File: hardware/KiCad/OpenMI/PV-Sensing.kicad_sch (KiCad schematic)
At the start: 16 parts

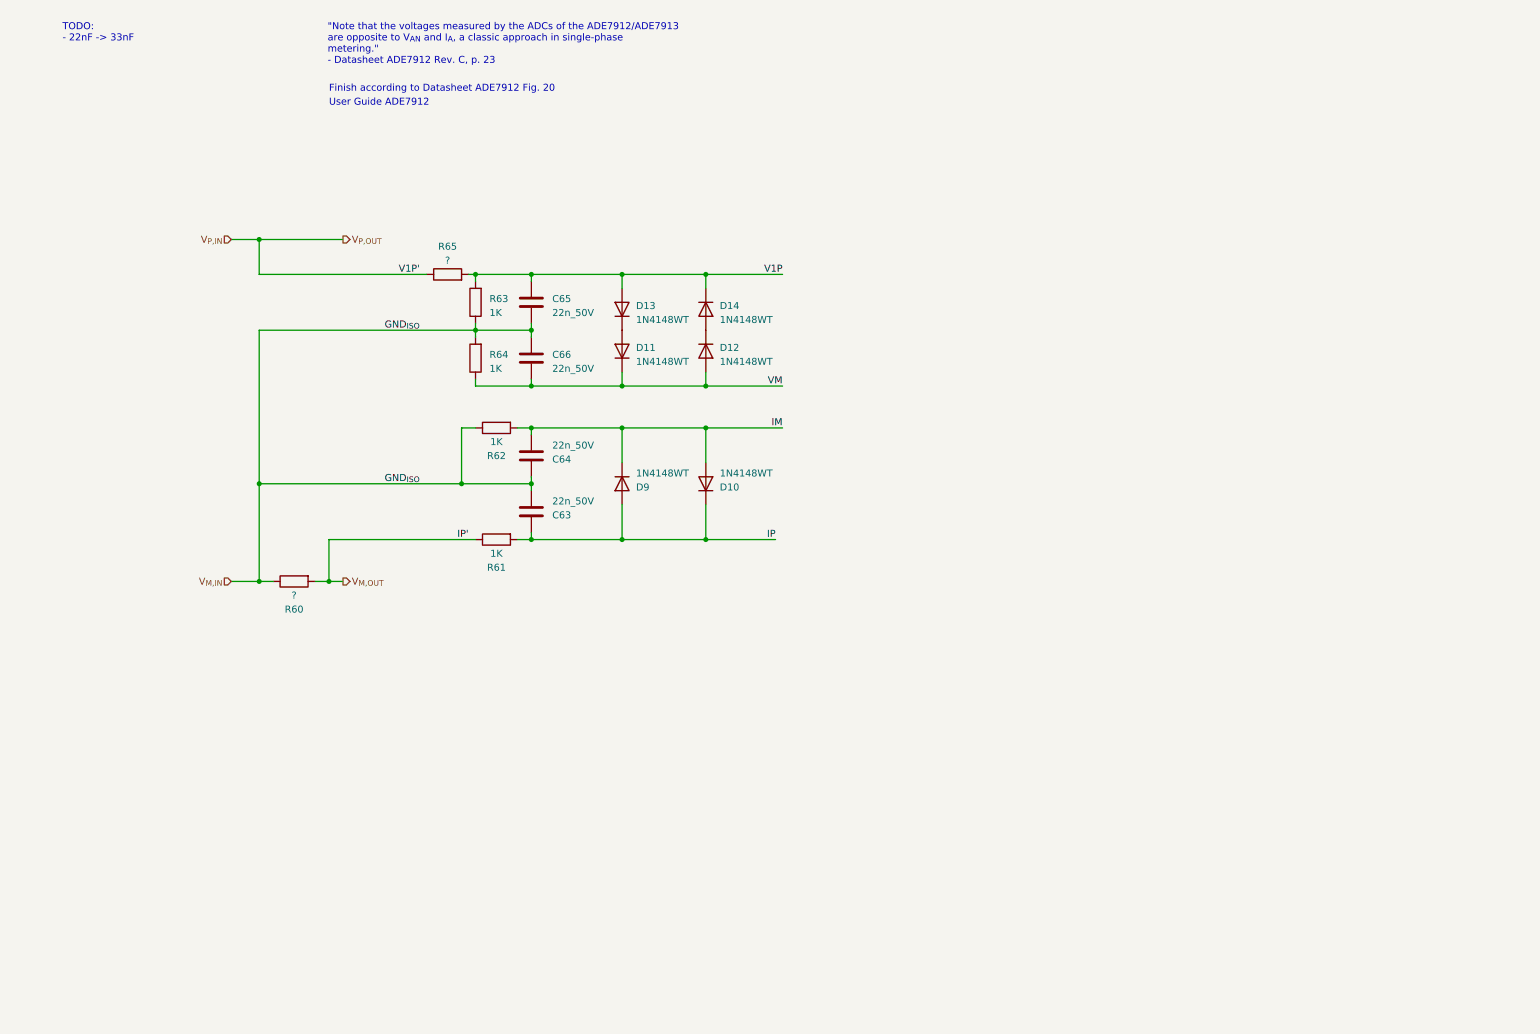
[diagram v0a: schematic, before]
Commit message: Adds specific values for sense resistors.
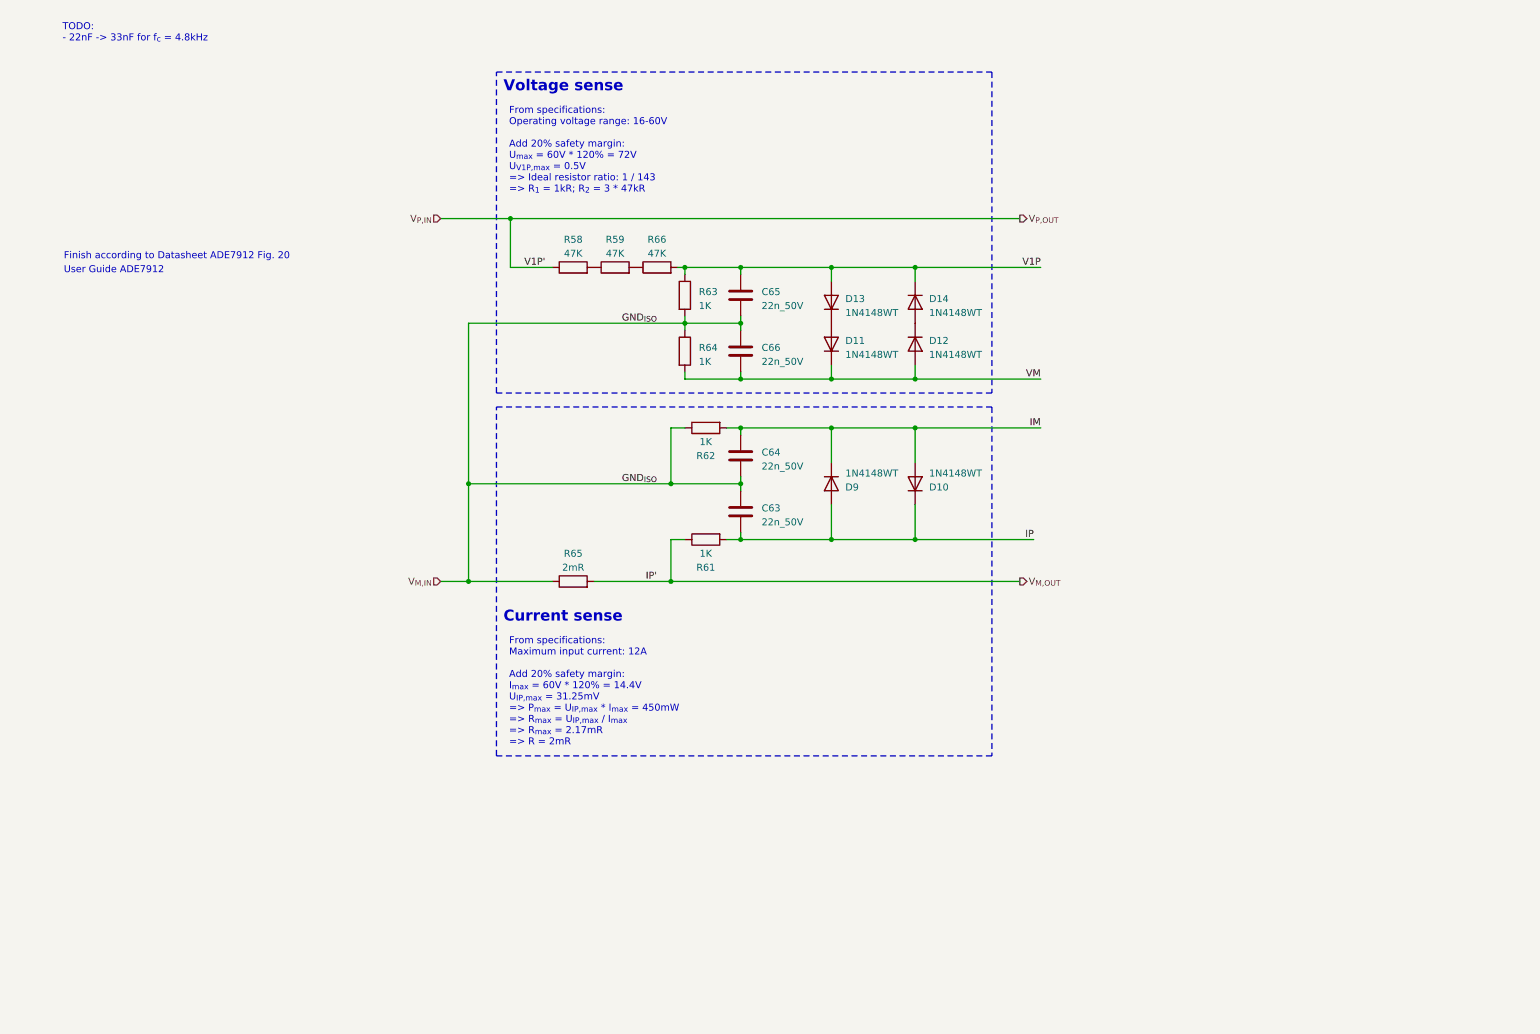
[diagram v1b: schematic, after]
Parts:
- removed R60: ?, Resistor_SMD:R_1206_3216Metric, symbol _R_1206:?
- removed R65: ?, Resistor_SMD:R_0805_2012Metric, symbol _R_0805:?
- added R58, R59, R66: 47K, Resistor_SMD:R_0603_1608Metric, symbol _R_0603:47K
- added R65: 2mR, Resistor_SMD:R_2512_6332Metric, symbol _R_2512:2mR
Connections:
- net IM: now also C64.1; no longer C64.2
- net IP: now also C63.2; no longer C63.1
- net V1P: now also R63.1, R66.2; no longer R63.2
- net VM: now also R64.2; no longer R64.1
- net V_{M,IN}: now also C63.1, C64.2, R63.2, R64.1, R65.1; no longer C63.2, C64.1, R63.1, R64.2
- net V_{M,OUT}: now also R65.2
- net V_{P,IN}: now also R58.1
- new net: R58.2, R59.1
- new net: R59.2, R66.1
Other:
- note added: "Current sense"
- note added: "Voltage sense"
- moved on the sheet: C63, C64, C65, C66, D10, D11, D12, D13, D14, D9, R61, R62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

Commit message: Set anti-aliasing cutoff frequency to 4.8kHz. Adds documentation.
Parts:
- removed C63, C64, C65, C66: 22n_50V, Capacitor_SMD:C_0603_1608Metric, symbol _C_0603:22n_50V
- added C63, C64, C65, C66: 33n_50V, Capacitor_SMD:C_0603_1608Metric, symbol _C_0603:33n_50V
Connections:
- net IM: now also C65.1
- net IP: now also C66.2
- net V1P: now also C63.1
- net VM: now also C64.2
- net V_{M,IN}: now also C63.2, C64.1, C65.2, C66.1
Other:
- note added: "Voltage & current sense"

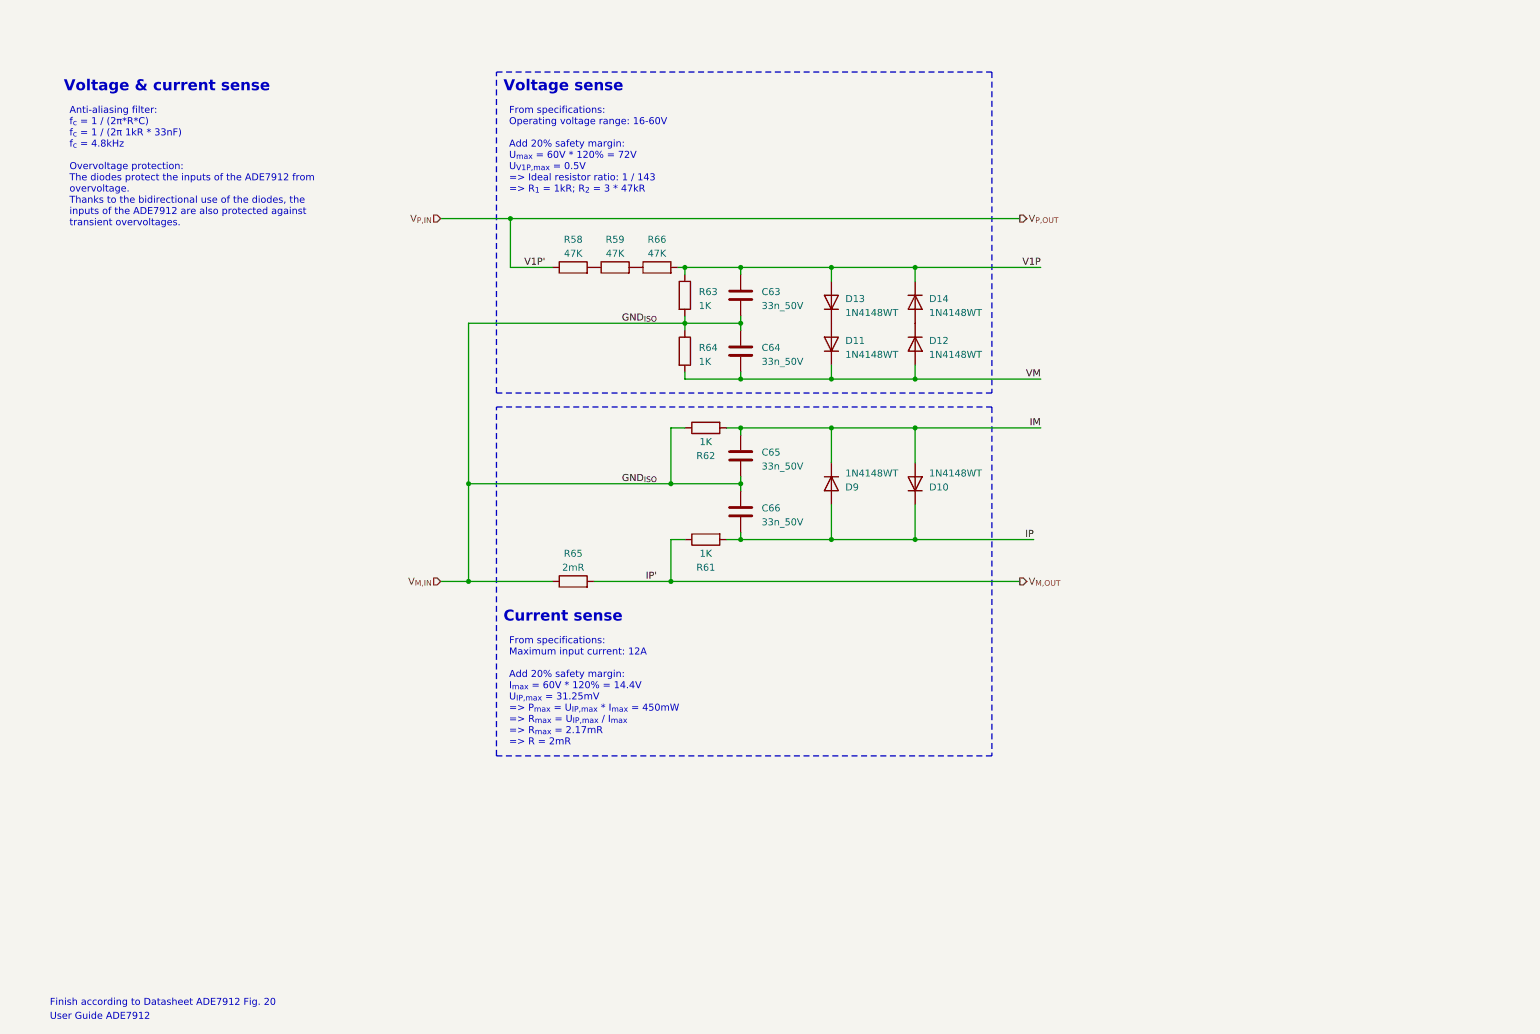
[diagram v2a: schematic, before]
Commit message: Adds ADE7912
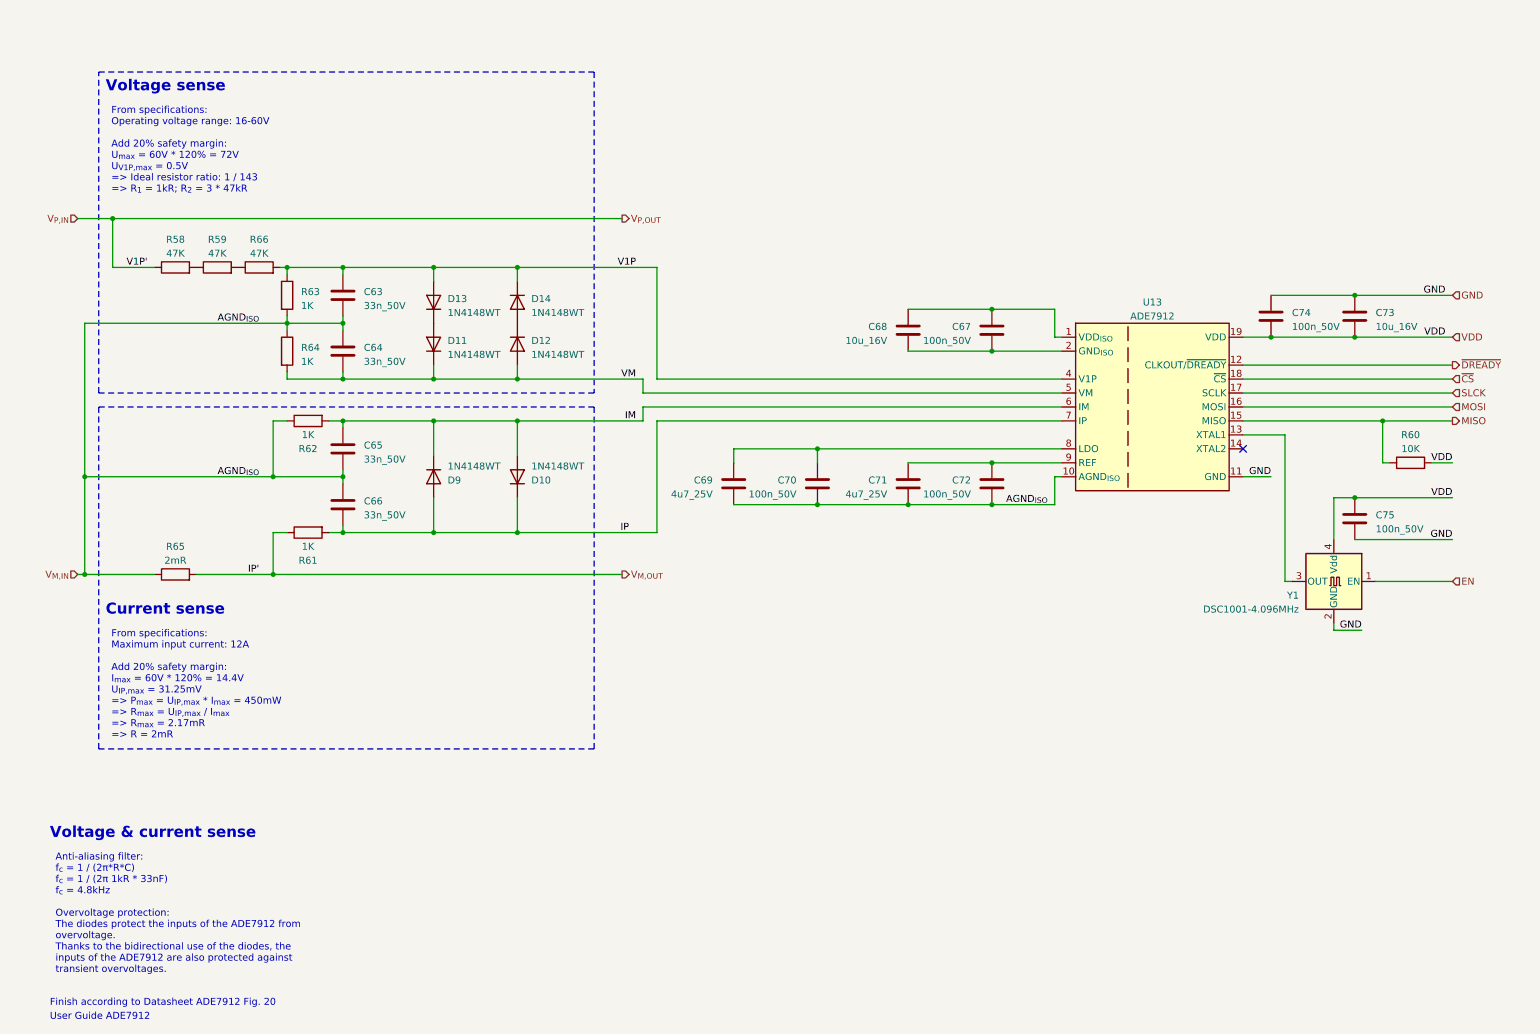
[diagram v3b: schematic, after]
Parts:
- added C67, C70, C72, C74, C75: 100n_50V, Capacitor_SMD:C_0603_1608Metric, symbol _C_0603:100n_50V
- added C68, C73: 10u_16V, Capacitor_SMD:C_0805_2012Metric, symbol _C_0805:10u_16V
- added C69, C71: 4u7_25V, Capacitor_SMD:C_0805_2012Metric, symbol _C_0805:4u7_25V
- added R60: 10K, Resistor_SMD:R_0603_1608Metric, symbol _R_0603:10K
- added U13: ADE7912, Package_SO:SOIC-20W_7.5x15.4mm_P1.27mm, symbol _Analog_ADC:ADE7912
- added Y1: DSC1001-4.096MHz, Oscillator:Oscillator_SMD_Abracon_ASE-4Pin_3.2x2.5mm, symbol _Oscillator:DSC1001-4.096MHz
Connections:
- net IM: now also U13.6 (IM)
- net IP: now also U13.7 (IP)
- net V1P: now also U13.4 (V1P)
- net VM: now also U13.3 (V2P), U13.5 (VM)
- net V_{M,IN}: now also C69.2, C70.2, C71.2, C72.2, U13.10 (AGND_{ISO})
- new net: C69.1, C70.1, U13.8 (LDO)
- new net: C67.1, C68.1, U13.1 (VDD_{ISO})
- new net: C67.2, C68.2, U13.2 (GND_{ISO})
- new net: U13.13 (XTAL1), Y1.3 (OUT)
- new net: C71.1, C72.1, U13.9 (REF)
- new net EN: Y1.1 (EN)
- new net GND: C73.1, C74.1, C75.2, U13.11 (GND), U13.20 (GND), Y1.2 (GND)
- new net MISO: R60.1, U13.15 (MISO)
- new net MOSI: U13.16 (MOSI)
- new net SLCK: U13.17 (SCLK)
- new net VDD: C73.2, C74.2, C75.1, R60.2, U13.19 (VDD), Y1.4 (Vdd)
- new net ~{CS}: U13.18 (~{CS})
- new net ~{DREADY}: U13.12 (CLKOUT/~{DREADY})
- no-connect marks 0 -> 1
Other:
- moved on the sheet: C63, C64, C65, C66, D10, D11, D12, D13, D14, D9, R58, R59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

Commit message: Tidy up schematics. Adds sheet symbols to root.
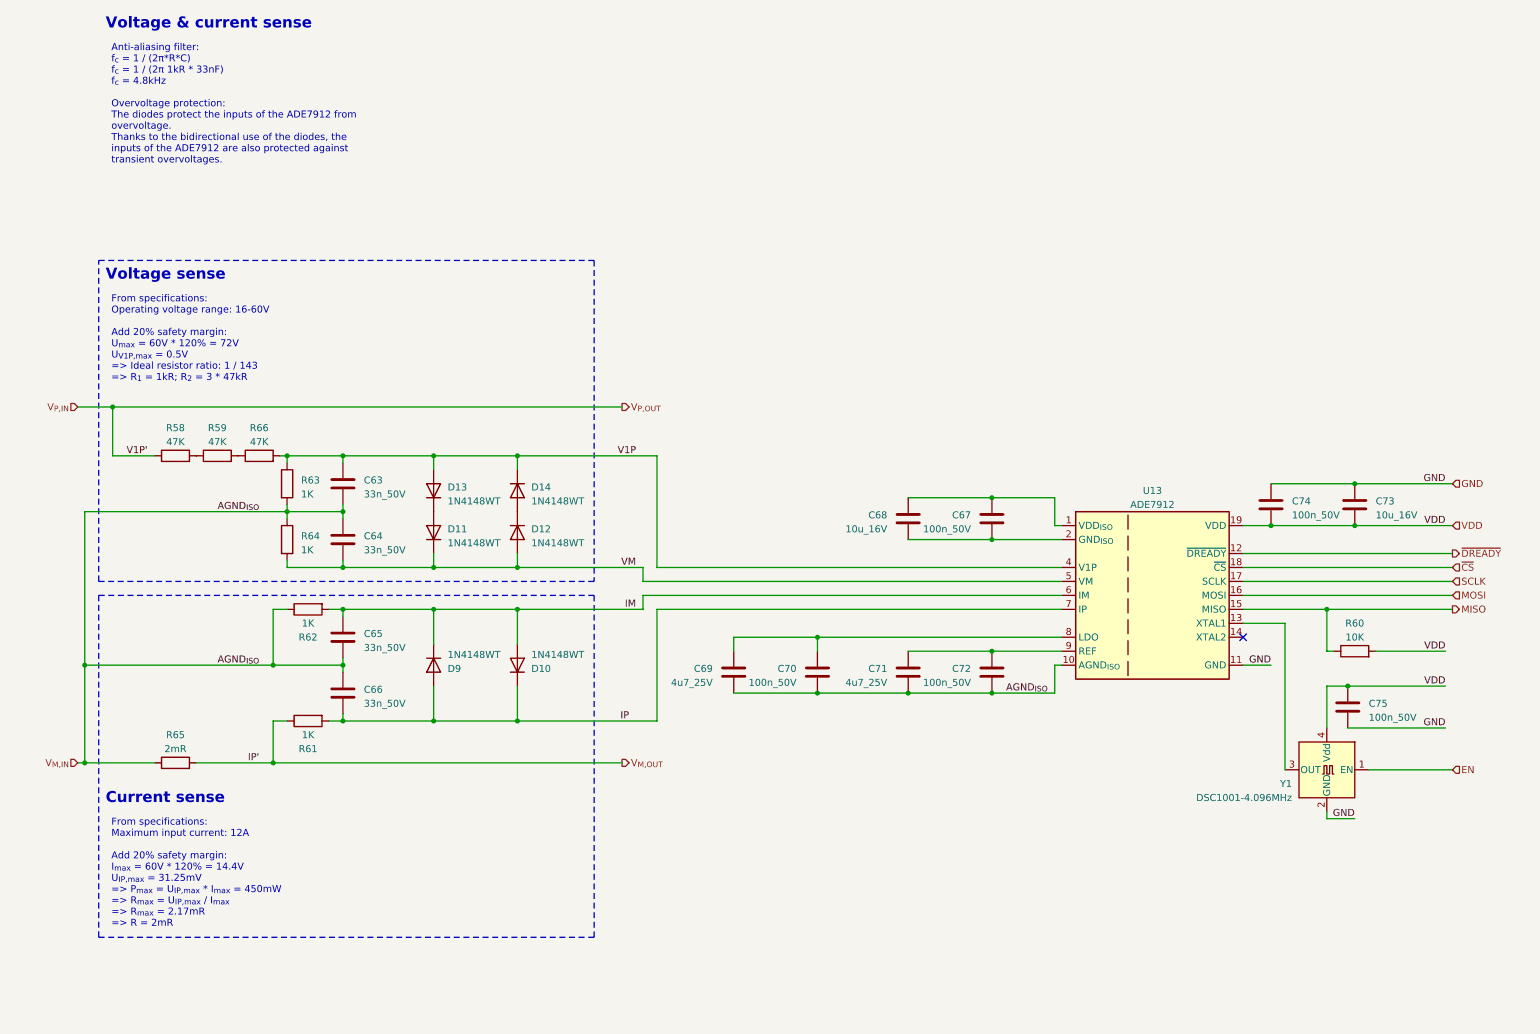
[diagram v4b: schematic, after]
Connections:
- net SLCK renamed SCLK
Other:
- note removed: "Finish according to Datasheet ADE7912 Fig. 20"
- note removed: "User Guide ADE7912"
- moved on the sheet: C63, C64, C65, C66, C67, C68, C69, C70, C71, C72, C73, C74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
